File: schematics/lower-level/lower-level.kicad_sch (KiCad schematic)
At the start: 17 parts, among them M1 Left EDF, M2 Right EDF, M3 AoA Servo MG996R, U1 STM32H743VGTx, U2 XGZP6847A, U3 XGZP6847A, U4 4525DO-DS5AI001DP, U5 ICM-42688-P, U6 MPXV7002DP, U7 MPXV7002DP, U8 BME280

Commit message: feat: schematics and basic driver code
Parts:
- added J1: TFmini-S, symbol Connector_Generic_MountingPin:Benewake TFmini-S
- added J2: UART to Application Chip, symbol Connector_Generic_Shielded:Conn_01x03_Shielded
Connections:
- net +3V3: now also D1.3 (VCC), D1.5 (VDD), U1.100 (VDD), U1.11 (VDD), U1.20 (VREF+), U1.21 (VDDA), U1.27 (VDD), U1.50 (VDD), U1.6 (VBAT), U1.75 (VDD), U2.2 (VDD), U2.4 (VDD), U3.2 (VDD), U3.4 (VDD), U4.2 (SUPPLY), U5.5 (VDDIO), U5.8 (VDD), U6.2 (VS), U7.2 (VS), U8.6 (VDDIO), U8.8 (VDD)
- net +5V: now also M3.2 (+), J1.1 (5V)
- net GND: now also D1.6 (VSS), M3.3 (-), MK1.3 (GND), U1.81 (PD0), U2.3 (GND), U2.5 (OUT), U2.6 (GND), U3.3 (GND), U3.6 (GND), U4.1 (GND), U5.6 (GND), U6.3 (GND), U7.3 (GND), J1.4 (GND), J2.3 (Pin_3)
- net at M3.1 (PWM): now also U1.22 (PA0)
- net at U1.18 (PC3_C): now also D1.2 (DIN)
- net at U1.24 (PA2): now also J2.1 (Pin_1)
- net at U1.25 (PA3): now also J2.2 (Pin_2)
- net at U1.39 (PE9): now also M1.1 (PWM)
- net at U1.40 (PE10): now also M2.1 (PWM)
- net at U1.51 (PB12): now also MK1.1 (WS)
- net at U1.52 (PB13): now also MK1.4 (SCK)
- net at U1.53 (PB14): now also MK1.6 (SD)
- net at U1.82 (PD1): now also U3.5 (OUT)
- net at U1.83 (PD2): now also U6.4 (VOUT)
- net at U1.84 (PD3): now also U7.4 (VOUT)
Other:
- moved on the sheet: MK1, U2

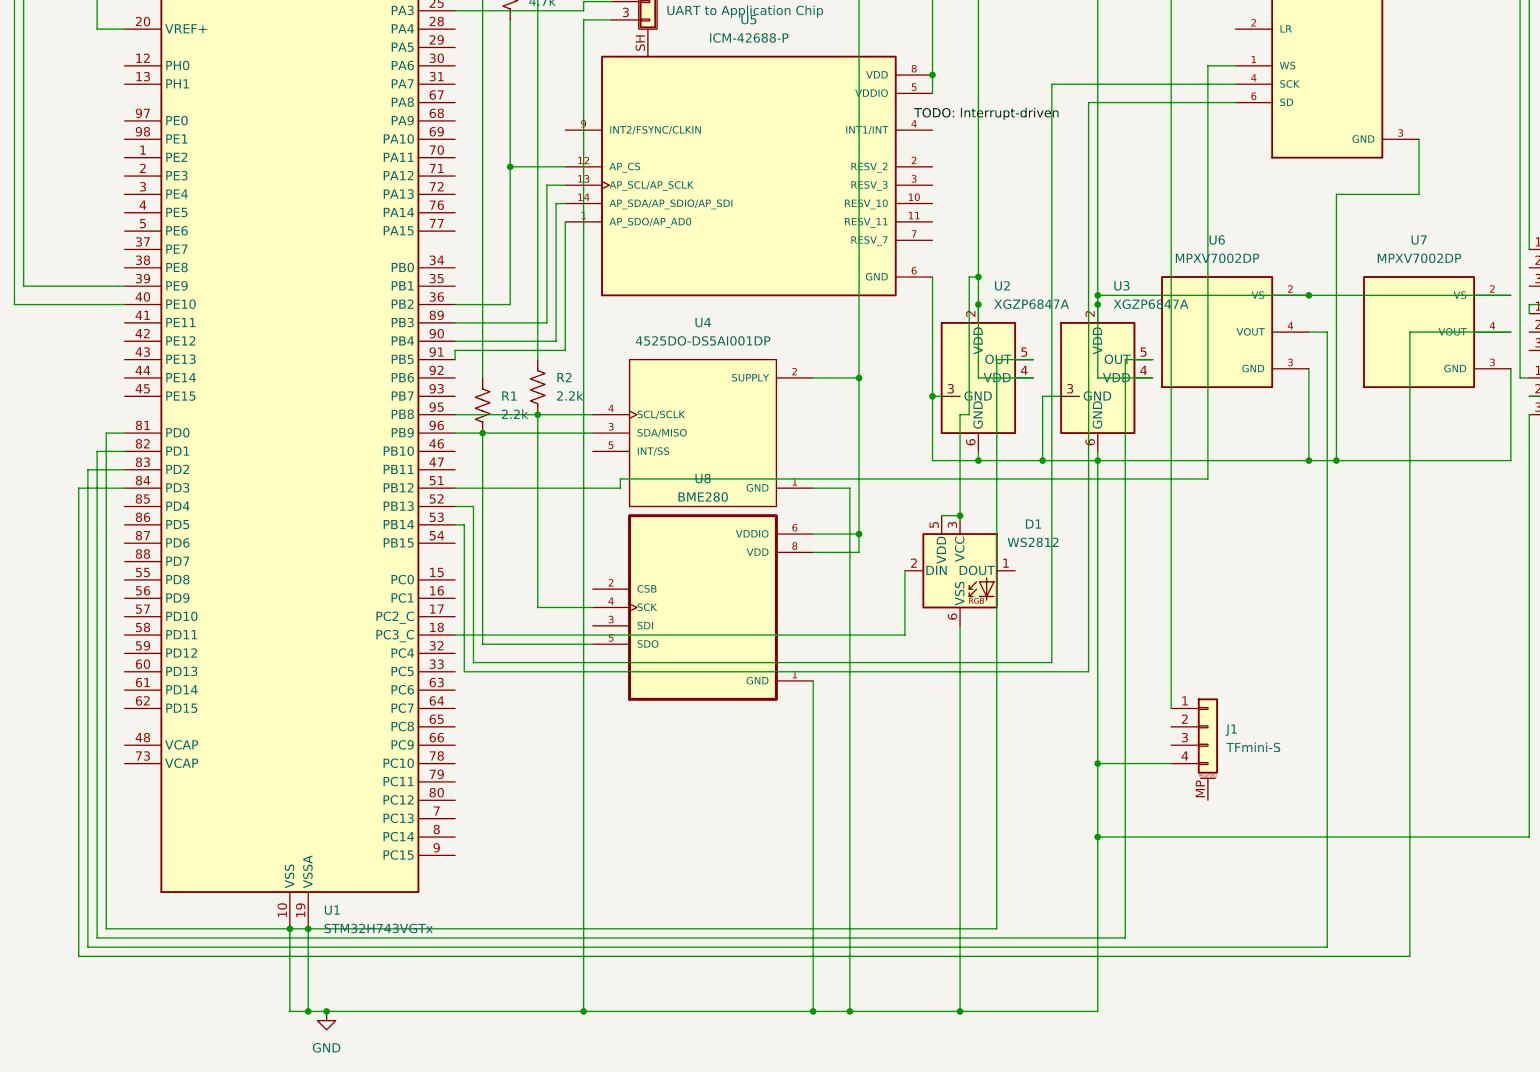
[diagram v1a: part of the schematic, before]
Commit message: refactor(firmware): send message should not block the mutex
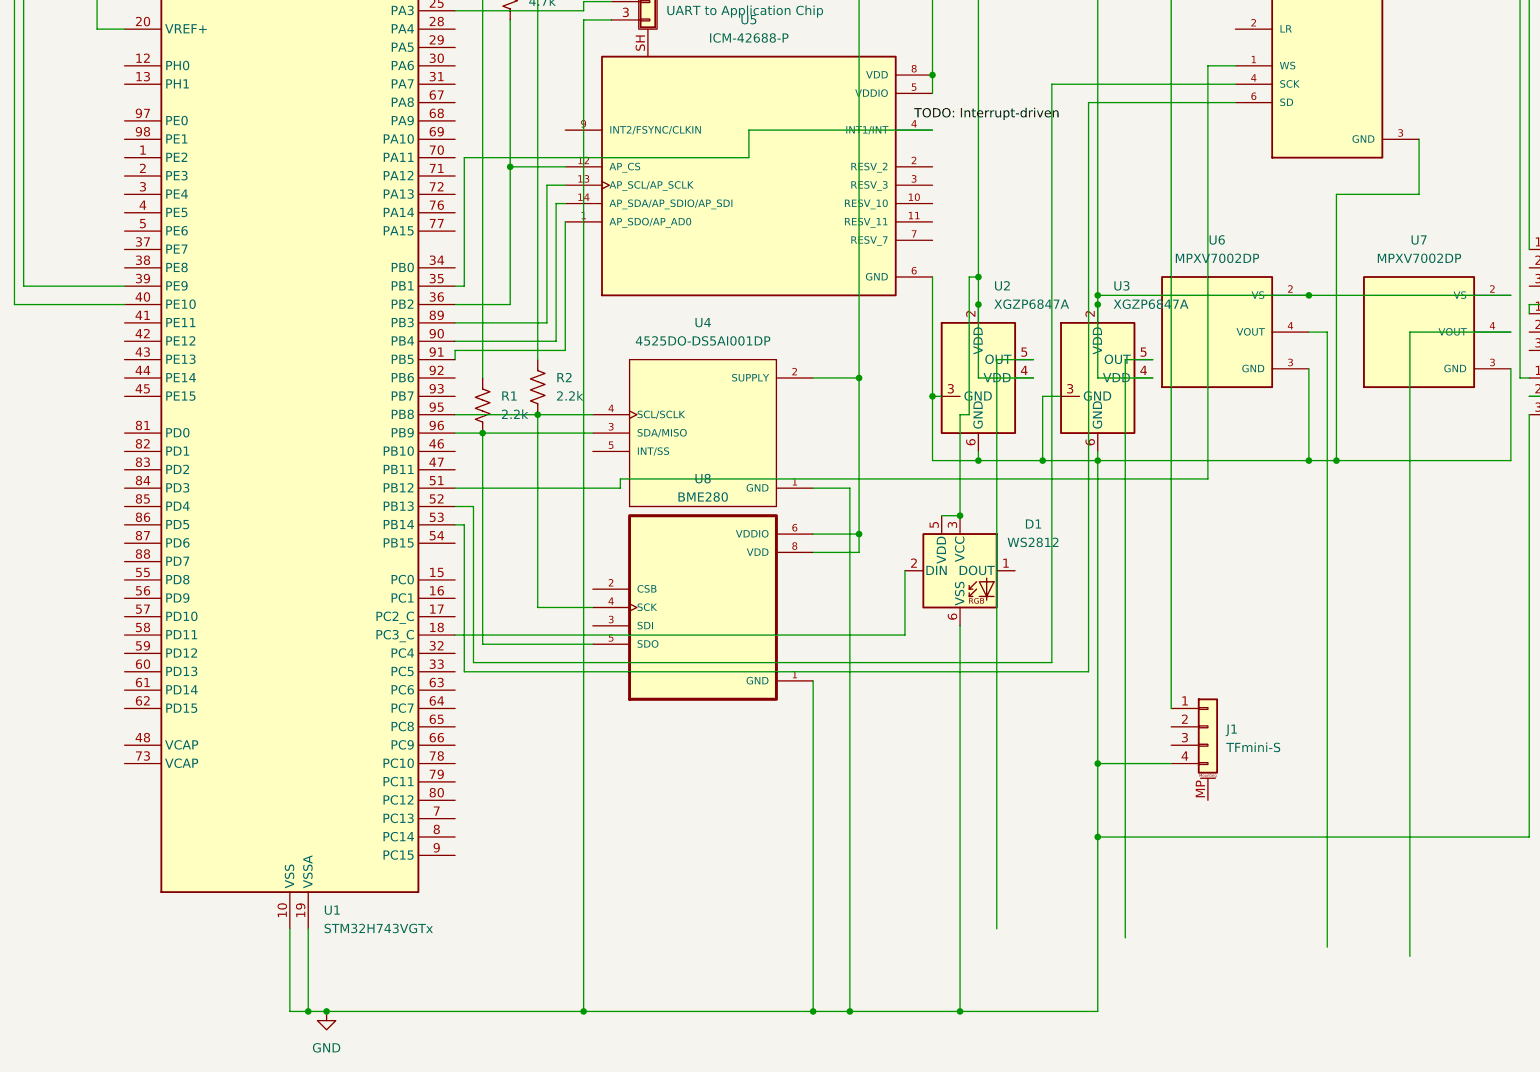
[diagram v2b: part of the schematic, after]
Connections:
- net GND: no longer U1.81 (PD0), U2.5 (OUT)
- net at U1.35 (PB1): now also U5.4 (INT1/INT)
- net at U1.82 (PD1): no longer U3.5 (OUT)
- net at U1.83 (PD2): no longer U6.4 (VOUT)
- net at U1.84 (PD3): no longer U7.4 (VOUT)
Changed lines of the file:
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@@
-	)
-	(junction
-		(at 58.42 173.99)
-		(diameter 0)
-		(color 0 0 0 0)
 	)
 	(junction
@@
 	)
 	(junction
-		(at 60.96 173.99)
-		(diameter 0)
-		(color 0 0 0 0)
-	)
-	(junction
 		(at 153.67 27.94)
 		(diameter 0)
@@
 	(wire
 		(pts
-			(xy 33.02 105.41) (xy 33.02 173.99)
-		)
-		(stroke
-			(width 0)
-			(type default)
-		)
-	)
-	(wire
-		(pts
 			(xy 95.25 73.66) (xy 95.25 92.71)
 		)
@@
 	(wire
 		(pts
-			(xy 60.96 173.99) (xy 156.21 173.99)
-		)
-		(stroke
-			(width 0)
-			(type default)
-		)
-	)
-	(wire
-		(pts
 			(xy 180.34 24.13) (xy 180.34 143.51)
 		)
@@
 	(wire
 		(pts
-			(xy 29.21 177.8) (xy 29.21 113.03)
-		)
-		(stroke
-			(width 0)
-			(type default)
-		)
-	)
-	(wire
-		(pts
 			(xy 153.67 109.22) (xy 162.56 109.22)
 		)
@@
 	(wire
 		(pts
-			(xy 29.21 113.03) (xy 35.56 113.03)
-		)
-		(stroke
-			(width 0)
-			(type default)
-		)
-	)
-	(wire
-		(pts
 			(xy 102.87 48.26) (xy 99.06 48.26)
 		)
@@
 	(wire
 		(pts
-			(xy 213.36 177.8) (xy 29.21 177.8)
-		)
-		(stroke
-			(width 0)
-			(type default)
-		)
-	)
-	(wire
-		(pts
 			(xy 35.56 87.63) (xy 20.32 87.63)
 		)
@@
 	(wire
 		(pts
+			(xy 82.55 85.09) (xy 81.28 85.09)
+		)
+		(stroke
+			(width 0)
+			(type default)
+		)
+	)
+	(wire
+		(pts
 			(xy 81.28 95.25) (xy 81.28 93.98)
 		)
@@
 	(wire
 		(pts
-			(xy 30.48 110.49) (xy 30.48 176.53)
-		)
-		(stroke
-			(width 0)
-			(type default)
-		)
-	)
-	(wire
-		(pts
 			(xy 165.1 100.33) (xy 162.56 100.33)
 		)
@@
 	(wire
 		(pts
+			(xy 147.32 63.5) (xy 121.92 63.5)
+		)
+		(stroke
+			(width 0)
+			(type default)
+		)
+	)
+	(wire
+		(pts
 			(xy 130.81 119.38) (xy 137.16 119.38)
 		)
@@
 	(wire
 		(pts
-			(xy 31.75 175.26) (xy 173.99 175.26)
-		)
-		(stroke
-			(width 0)
-			(type default)
-		)
-	)
-	(wire
-		(pts
-			(xy 30.48 176.53) (xy 201.93 176.53)
-		)
-		(stroke
-			(width 0)
-			(type default)
-		)
-	)
-	(wire
-		(pts
 			(xy 58.42 185.42) (xy 60.96 185.42)
 		)
@@
 	(wire
 		(pts
+			(xy 82.55 67.31) (xy 82.55 85.09)
+		)
+		(stroke
+			(width 0)
+			(type default)
+		)
+	)
+	(wire
+		(pts
 			(xy 100.33 134.62) (xy 85.09 134.62)
 		)
@@
 	(wire
 		(pts
-			(xy 35.56 107.95) (xy 31.75 107.95)
-		)
-		(stroke
-			(width 0)
-			(type default)
-		)
-	)
-	(wire
-		(pts
-			(xy 58.42 173.99) (xy 60.96 173.99)
-		)
-		(stroke
-			(width 0)
-			(type default)
-		)
-	)
-	(wire
-		(pts
 			(xy 151.13 132.08) (xy 151.13 185.42)
 		)
@@
 	(wire
 		(pts
-			(xy 31.75 107.95) (xy 31.75 175.26)
-		)
-		(stroke
-			(width 0)
-			(type default)
-		)
-	)
-	(wire
-		(pts
 			(xy 93.98 71.12) (xy 93.98 90.17)
 		)
@@
 	(wire
 		(pts
+			(xy 121.92 63.5) (xy 121.92 67.31)
+		)
+		(stroke
+			(width 0)
+			(type default)
+		)
+	)
+	(wire
+		(pts
 			(xy 137.16 27.94) (xy 92.71 27.94)
 		)
@@
 	(wire
 		(pts
-			(xy 35.56 105.41) (xy 33.02 105.41)
-		)
-		(stroke
-			(width 0)
-			(type default)
-		)
-	)
-	(wire
-		(pts
-			(xy 33.02 173.99) (xy 58.42 173.99)
-		)
-		(stroke
-			(width 0)
-			(type default)
-		)
-	)
-	(wire
-		(pts
-			(xy 35.56 110.49) (xy 30.48 110.49)
-		)
-		(stroke
-			(width 0)
-			(type default)
-		)
-	)
-	(wire
-		(pts
 			(xy 50.8 29.21) (xy 50.8 27.94)
 		)
@@
 		)
 		(stroke
+			(width 0)
+			(type default)
+		)
+	)
+	(wire
+		(pts
+			(xy 121.92 67.31) (xy 82.55 67.31)
+		)
+		(stroke
